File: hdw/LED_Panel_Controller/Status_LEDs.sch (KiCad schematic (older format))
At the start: 20 parts

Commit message: lots of schematic progress
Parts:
- removed U? (x4): 74LVC1G06, TO_SOT_Packages_SMD:SOT-353_SC-70-5, symbol Custom_Library:74LVC1G06_Power
- added U? (x4): 74LVC1G97, Package_TO_SOT_SMD:SOT-363_SC-70-6, symbol Custom_Library:74LVC1G97_Power_NOT
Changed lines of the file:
@@
 encoding utf-8
 Sheet 19 34
-Title "Pulse Oximeter"
-Date "2020-08-01"
+Title "LED Panel Controller"
+Date "2020-12-23"
 Rev "A"
-Comp "Drew Maatman"
+Comp "Drew Maatman, Logan Wedel"
 Comment1 ""
 Comment2 ""
@@
 	1    0    0    -1
 $EndComp
-$Comp
-L Custom_Library:74LVC1G06_Power U?
-U 1 1 5EBB3661
-P 4390 2530
-AR Path="/5EAE4ADE/5EBB3661" Ref="U?"  Part="1"
-AR Path="/5EAE4AE4/5EBB3661" Ref="U?"  Part="1"
-AR Path="/5F582E50/5EBB3661" Ref="U?"  Part="1"
-F 0 "U?" H 4490 2680 50  0000 L CNN
-F 1 "74LVC1G06" H 4490 2430 50  0000 L CNN
-F 2 "TO_SOT_Packages_SMD:SOT-353_SC-70-5" H 4390 2580 50  0001 C CNN
-F 3 "http://www.ti.com/lit/ds/symlink/sn74lvc1g06.pdf" H 4390 2530 50  0001 C CNN
-F 4 "296-8484-1-ND" H 4390 2530 50  0001 C CNN "Digi-Key PN"
-	1    4390 2530
-	1    0    0    -1
-$EndComp
-$Comp
-L Custom_Library:74LVC1G06_Power U?
-U 1 1 5EBB3BCA
-P 6390 2530
-AR Path="/5EAE4ADE/5EBB3BCA" Ref="U?"  Part="1"
-AR Path="/5EAE4AE4/5EBB3BCA" Ref="U?"  Part="1"
-AR Path="/5F582E50/5EBB3BCA" Ref="U?"  Part="1"
-F 0 "U?" H 6490 2680 50  0000 L CNN
-F 1 "74LVC1G06" H 6490 2430 50  0000 L CNN
-F 2 "TO_SOT_Packages_SMD:SOT-353_SC-70-5" H 6390 2580 50  0001 C CNN
-F 3 "http://www.ti.com/lit/ds/symlink/sn74lvc1g06.pdf" H 6390 2530 50  0001 C CNN
-F 4 "296-8484-1-ND" H 6390 2530 50  0001 C CNN "Digi-Key PN"
-	1    6390 2530
-	1    0    0    -1
-$EndComp
-$Comp
-L Custom_Library:74LVC1G06_Power U?
-U 1 1 5EBB56C7
-P 6390 4530
-AR Path="/5EAE4ADE/5EBB56C7" Ref="U?"  Part="1"
-AR Path="/5EAE4AE4/5EBB56C7" Ref="U?"  Part="1"
-AR Path="/5F582E50/5EBB56C7" Ref="U?"  Part="1"
-F 0 "U?" H 6490 4680 50  0000 L CNN
-F 1 "74LVC1G06" H 6490 4430 50  0000 L CNN
-F 2 "TO_SOT_Packages_SMD:SOT-353_SC-70-5" H 6390 4580 50  0001 C CNN
-F 3 "http://www.ti.com/lit/ds/symlink/sn74lvc1g06.pdf" H 6390 4530 50  0001 C CNN
-F 4 "296-8484-1-ND" H 6390 4530 50  0001 C CNN "Digi-Key PN"
-	1    6390 4530
-	1    0    0    -1
-$EndComp
-$Comp
-L Custom_Library:74LVC1G06_Power U?
-U 1 1 5EBB6CE5
-P 4390 4530
-AR Path="/5EAE4ADE/5EBB6CE5" Ref="U?"  Part="1"
-AR Path="/5EAE4AE4/5EBB6CE5" Ref="U?"  Part="1"
-AR Path="/5F582E50/5EBB6CE5" Ref="U?"  Part="1"
-F 0 "U?" H 4490 4680 50  0000 L CNN
-F 1 "74LVC1G06" H 4490 4430 50  0000 L CNN
-F 2 "TO_SOT_Packages_SMD:SOT-353_SC-70-5" H 4390 4580 50  0001 C CNN
-F 3 "http://www.ti.com/lit/ds/symlink/sn74lvc1g06.pdf" H 4390 4530 50  0001 C CNN
-F 4 "296-8484-1-ND" H 4390 4530 50  0001 C CNN "Digi-Key PN"
-	1    4390 4530
-	1    0    0    -1
-$EndComp
 Text GLabel 3760 4530 0    50   Input ~ 0
 Error_LED
+$Comp
+L Custom_Library:74LVC1G97_Power_NOT U?
+U 1 1 5FE90879
+P 4390 2530
+F 0 "U?" H 4450 2680 50  0000 L CNN
+F 1 "74LVC1G97" H 4450 2380 50  0000 L CNN
+F 2 "Package_TO_SOT_SMD:SOT-363_SC-70-6" H 4440 2530 50  0001 C CNN
+F 3 "http://www.ti.com/lit/ds/symlink/sn74lvc1g97.pdf" H 4440 2530 50  0001 C CNN
+	1    4390 2530
+	1    0    0    -1
+$EndComp
+$Comp
+L Custom_Library:74LVC1G97_Power_NOT U?
+U 1 1 5FE90D68
+P 6390 2530
+F 0 "U?" H 6450 2680 50  0000 L CNN
+F 1 "74LVC1G97" H 6450 2380 50  0000 L CNN
+F 2 "Package_TO_SOT_SMD:SOT-363_SC-70-6" H 6440 2530 50  0001 C CNN
+F 3 "http://www.ti.com/lit/ds/symlink/sn74lvc1g97.pdf" H 6440 2530 50  0001 C CNN
+	1    6390 2530
+	1    0    0    -1
+$EndComp
+$Comp
+L Custom_Library:74LVC1G97_Power_NOT U?
+U 1 1 5FE91396
+P 4390 4530
+F 0 "U?" H 4450 4680 50  0000 L CNN
+F 1 "74LVC1G97" H 4450 4380 50  0000 L CNN
+F 2 "Package_TO_SOT_SMD:SOT-363_SC-70-6" H 4440 4530 50  0001 C CNN
+F 3 "http://www.ti.com/lit/ds/symlink/sn74lvc1g97.pdf" H 4440 4530 50  0001 C CNN
+	1    4390 4530
+	1    0    0    -1
+$EndComp
+$Comp
+L Custom_Library:74LVC1G97_Power_NOT U?
+U 1 1 5FE9193A
+P 6390 4530
+F 0 "U?" H 6450 4680 50  0000 L CNN
+F 1 "74LVC1G97" H 6450 4380 50  0000 L CNN
+F 2 "Package_TO_SOT_SMD:SOT-363_SC-70-6" H 6440 4530 50  0001 C CNN
+F 3 "http://www.ti.com/lit/ds/symlink/sn74lvc1g97.pdf" H 6440 4530 50  0001 C CNN
+	1    6390 4530
+	1    0    0    -1
+$EndComp
 $EndSCHEMATC

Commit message: added digikey pns, footprints, bom scrubbed
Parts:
- R? (x4): Digi-Key PN (none) -> RMCF0402FT1K00CT-ND
- U? (x4): Digi-Key PN (none) -> 1727-1772-1-ND
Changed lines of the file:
@@
 F 5 "1%" H 5030 1960 50  0000 L CNN "Tolerance"
 F 6 "1/16W" H 5030 1890 50  0000 L CNN "Wattage"
-F 7 "" H 5260 2360 60  0001 C CNN "Digi-Key PN"
+F 7 "RMCF0402FT1K00CT-ND" H 5260 2360 60  0001 C CNN "Digi-Key PN"
 	1    4960 1960
 	-1   0    0    -1
@@
 F 5 "1%" H 7030 1960 50  0000 L CNN "Tolerance"
 F 6 "1/16W" H 7030 1890 50  0000 L CNN "Wattage"
-F 7 "" H 7260 2360 60  0001 C CNN "Digi-Key PN"
+F 7 "RMCF0402FT1K00CT-ND" H 7260 2360 60  0001 C CNN "Digi-Key PN"
 	1    6960 1960
 	-1   0    0    -1
@@
 F 5 "1%" H 7030 3960 50  0000 L CNN "Tolerance"
 F 6 "1/16W" H 7030 3890 50  0000 L CNN "Wattage"
-F 7 "" H 7260 4360 60  0001 C CNN "Digi-Key PN"
+F 7 "RMCF0402FT1K00CT-ND" H 7260 4360 60  0001 C CNN "Digi-Key PN"
 	1    6960 3960
 	-1   0    0    -1
@@
 F 5 "1%" H 5030 3960 50  0000 L CNN "Tolerance"
 F 6 "1/16W" H 5030 3890 50  0000 L CNN "Wattage"
-F 7 "" H 5260 4360 60  0001 C CNN "Digi-Key PN"
+F 7 "RMCF0402FT1K00CT-ND" H 5260 4360 60  0001 C CNN "Digi-Key PN"
 	1    4960 3960
 	-1   0    0    -1
@@
 F 2 "Package_TO_SOT_SMD:SOT-363_SC-70-6" H 4440 2530 50  0001 C CNN
 F 3 "http://www.ti.com/lit/ds/symlink/sn74lvc1g97.pdf" H 4440 2530 50  0001 C CNN
+F 4 "1727-1772-1-ND" H 4390 2530 50  0001 C CNN "Digi-Key PN"
 	1    4390 2530
 	1    0    0    -1
@@
 F 2 "Package_TO_SOT_SMD:SOT-363_SC-70-6" H 6440 2530 50  0001 C CNN
 F 3 "http://www.ti.com/lit/ds/symlink/sn74lvc1g97.pdf" H 6440 2530 50  0001 C CNN
+F 4 "1727-1772-1-ND" H 6390 2530 50  0001 C CNN "Digi-Key PN"
 	1    6390 2530
 	1    0    0    -1
@@
 F 2 "Package_TO_SOT_SMD:SOT-363_SC-70-6" H 4440 4530 50  0001 C CNN
 F 3 "http://www.ti.com/lit/ds/symlink/sn74lvc1g97.pdf" H 4440 4530 50  0001 C CNN
+F 4 "1727-1772-1-ND" H 4390 4530 50  0001 C CNN "Digi-Key PN"
 	1    4390 4530
 	1    0    0    -1
@@
 F 2 "Package_TO_SOT_SMD:SOT-363_SC-70-6" H 6440 4530 50  0001 C CNN
 F 3 "http://www.ti.com/lit/ds/symlink/sn74lvc1g97.pdf" H 6440 4530 50  0001 C CNN
+F 4 "1727-1772-1-ND" H 6390 4530 50  0001 C CNN "Digi-Key PN"
 	1    6390 4530
 	1    0    0    -1

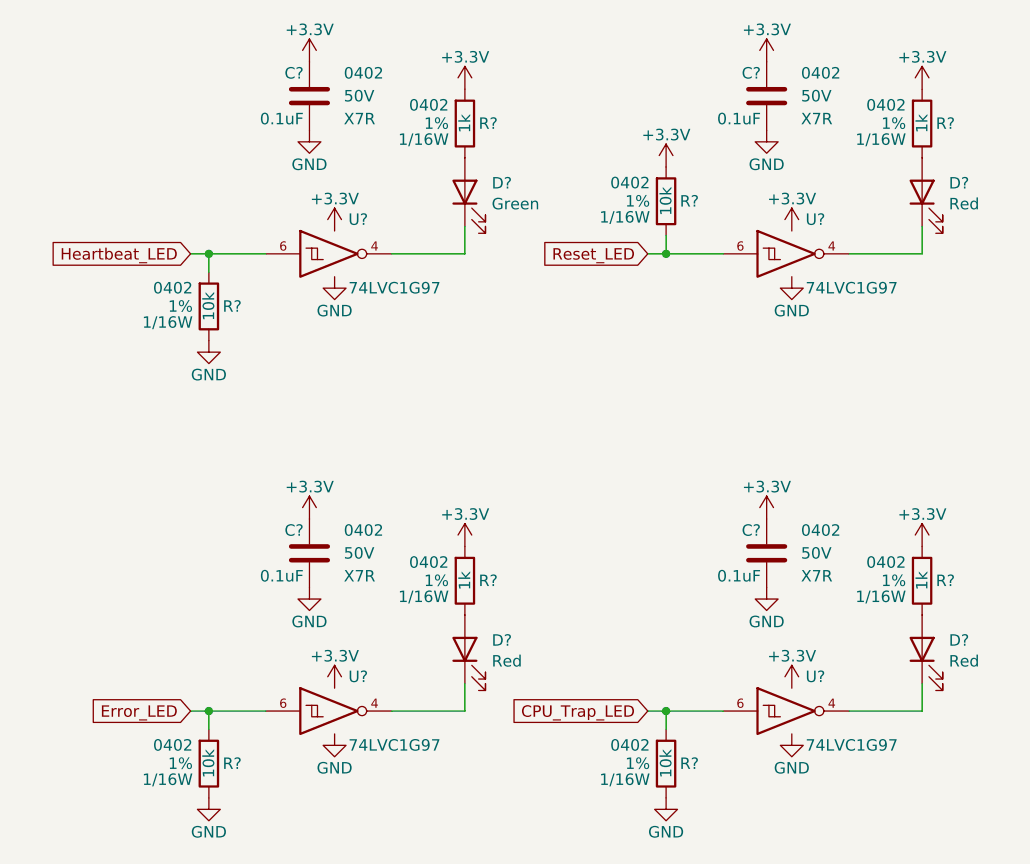
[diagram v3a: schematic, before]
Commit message: assigned I2C addresses
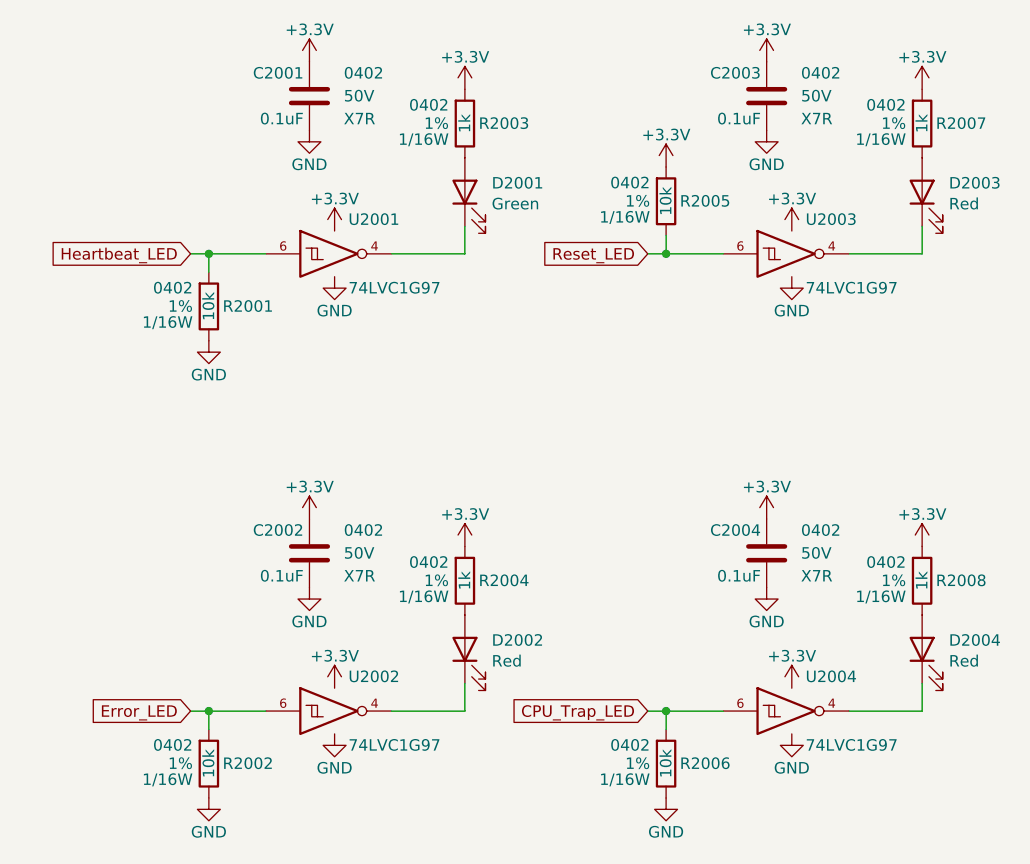
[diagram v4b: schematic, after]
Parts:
- gave numbers to parts that had none: 20

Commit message: added BOMs, some consolidation
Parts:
- C2001, C2002, C2003, C2004: Digi-Key PN 490-10701-1-ND -> 490-10698-1-ND
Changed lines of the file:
@@
 F 2 "Capacitors_SMD:C_0402" H 4318 1690 50  0001 C CNN
 F 3 "" H 4305 1940 50  0001 C CNN
-F 4 "490-10701-1-ND" H 4705 2340 60  0001 C CNN "Digi-Key PN"
+F 4 "490-10698-1-ND" H 4705 2340 60  0001 C CNN "Digi-Key PN"
 F 5 "0402" H 4130 1940 50  0000 R CNN "display_footprint"
 F 6 "50V" H 4130 1840 50  0000 R CNN "Voltage"
@@
 F 2 "Capacitors_SMD:C_0402" H 6318 1690 50  0001 C CNN
 F 3 "" H 6305 1940 50  0001 C CNN
-F 4 "490-10701-1-ND" H 6705 2340 60  0001 C CNN "Digi-Key PN"
+F 4 "490-10698-1-ND" H 6705 2340 60  0001 C CNN "Digi-Key PN"
 F 5 "0402" H 6130 1940 50  0000 R CNN "display_footprint"
 F 6 "50V" H 6130 1840 50  0000 R CNN "Voltage"
@@
 F 2 "Capacitors_SMD:C_0402" H 6318 3690 50  0001 C CNN
 F 3 "" H 6305 3940 50  0001 C CNN
-F 4 "490-10701-1-ND" H 6705 4340 60  0001 C CNN "Digi-Key PN"
+F 4 "490-10698-1-ND" H 6705 4340 60  0001 C CNN "Digi-Key PN"
 F 5 "0402" H 6130 3940 50  0000 R CNN "display_footprint"
 F 6 "50V" H 6130 3840 50  0000 R CNN "Voltage"
@@
 F 2 "Capacitors_SMD:C_0402" H 4318 3690 50  0001 C CNN
 F 3 "" H 4305 3940 50  0001 C CNN
-F 4 "490-10701-1-ND" H 4705 4340 60  0001 C CNN "Digi-Key PN"
+F 4 "490-10698-1-ND" H 4705 4340 60  0001 C CNN "Digi-Key PN"
 F 5 "0402" H 4130 3940 50  0000 R CNN "display_footprint"
 F 6 "50V" H 4130 3840 50  0000 R CNN "Voltage"
